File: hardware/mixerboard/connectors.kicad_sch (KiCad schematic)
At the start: 3 parts, among them J1 Eurorack Power, J2 IOBoard Upper, J3 IOBoard Lower

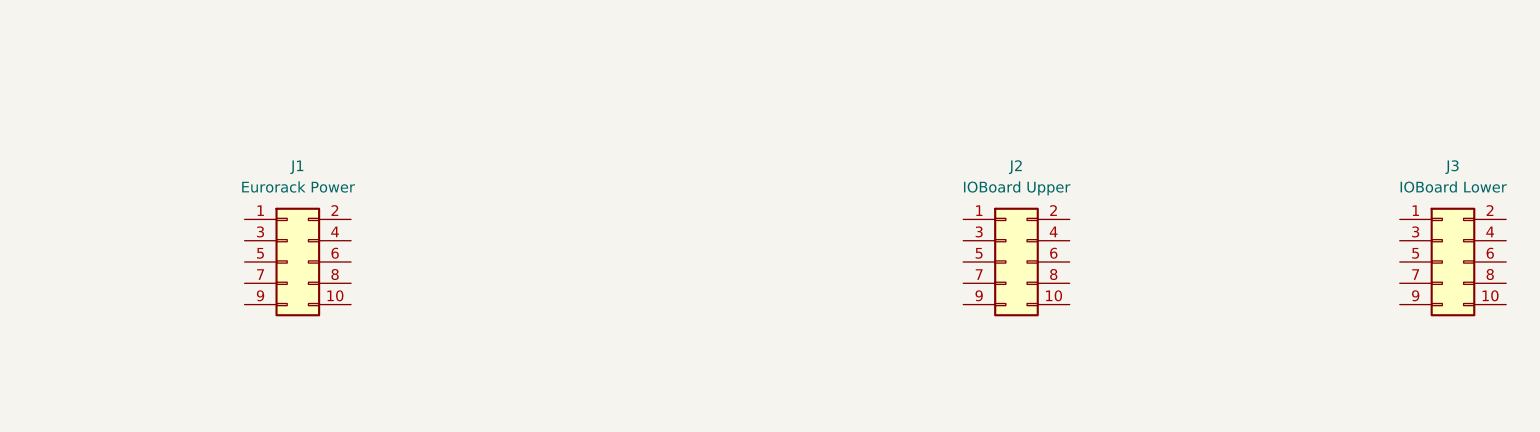
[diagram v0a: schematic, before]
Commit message: Add Eurorack power
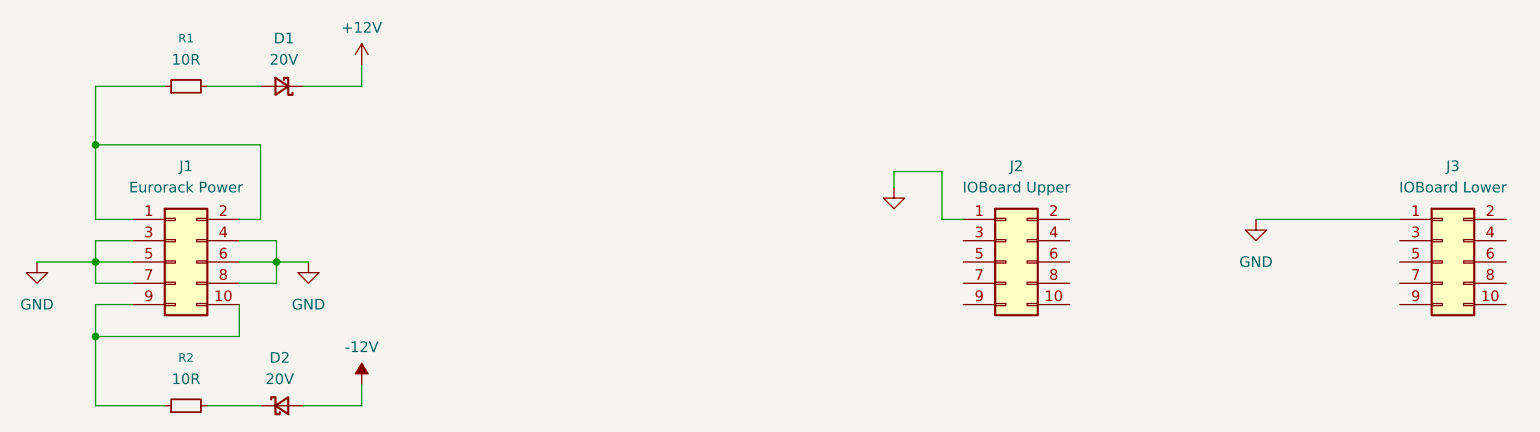
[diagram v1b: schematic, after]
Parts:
- added D1, D2: 20V, symbol Device:D_Schottky_Small
- added R1, R2: 10R, symbol Device:R_Small
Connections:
- net GND: now reaches J2.1 (Pin_1)
- net GND: now also J1.3 (Pin_3), J1.4 (Pin_4), J1.5 (Pin_5), J1.6 (Pin_6), J1.7 (Pin_7), J1.8 (Pin_8), J3.1 (Pin_1)
- net at J1.1 (Pin_1): now also J1.2 (Pin_2), R1.1
- net at J1.10 (Pin_10): now also J1.9 (Pin_9), R2.1
- new net: D2.1 (K), R2.2
- new net: D1.2 (A), R1.2
- new net +12V: D1.1 (K)
- new net -12V: D2.2 (A)
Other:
- moved on the sheet: J1
